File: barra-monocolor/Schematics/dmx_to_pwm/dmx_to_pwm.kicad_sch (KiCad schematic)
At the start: 54 parts, among them J1 RJ45, J2 RJ45, J3 Conn_01x05_Socket, J4 Conn_02x04_Odd_Even, Q1 BD237, Q2 BD237, Q3 BD237, Q4 BD237, SW1 SW_DIP_x08, U1 LM317_TO-220, U2 LM2596T-5, U3 LM337_TO220, U4 LM337_TO220, U5 LM337_TO220, U6 LM337_TO220, U7 SN75176AP, U8 H11L1

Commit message: first pcb layout
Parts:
- removed C10, C11, C8, C9: 1uF, symbol Device:C_Polarized
- removed C2, C3, C4, C5: 100nF, symbol Device:C_Polarized
- removed C6: C_Polarized, symbol Device:C_Polarized
- removed D1, D3, D4, D5, D6: D, symbol Device:D
- removed J3: Conn_01x05_Socket, symbol Connector:Conn_01x05_Socket
- removed J4: Conn_02x04_Odd_Even, symbol Connector_Generic:Conn_02x04_Odd_Even
- removed L1: 100 uH, symbol Device:L
- removed Q1, Q2, Q3, Q4: BD237, Package_TO_SOT_THT:TO-126-3_Vertical, symbol Transistor_BJT:BD237
- removed R11, R12: 470, Resistor_THT:R_Axial_DIN0204_L3.6mm_D1.6mm_P7.62mm_Horizontal, symbol Device:R_US
- removed R5: 8, symbol Device:R_US
- removed R6, R7, R8, R9: 2.7, symbol Device:R
- removed SW1: SW_DIP_x08, symbol Switch:SW_DIP_x08
- removed U1: LM317_TO-220, Package_TO_SOT_THT:TO-220-3_Vertical, symbol Regulator_Linear:LM317_TO-220
- removed U7: SN75176AP, Package_DIP:DIP-8_W7.62mm, symbol Interface_UART:SN75176AP
- removed U8: H11L1, symbol Isolator:H11L1
- added C10, C11, C8, C9: 1uF, Capacitor_THT:C_Disc_D3.0mm_W2.0mm_P2.50mm, symbol Device:C
- added C2, C3, C4, C5: 100nF, Capacitor_THT:C_Disc_D3.0mm_W2.0mm_P2.50mm, symbol Device:C
- added D3, D4, D5, D6: 1N4004, Diode_THT:D_DO-41_SOD81_P7.62mm_Horizontal, symbol Diode:1N4004
- added J3: Conn_02x04_Top_Bottom, Connector_PinHeader_2.54mm:PinHeader_2x04_P2.54mm_Vertical, symbol Connector_Generic:Conn_02x04_Top_Bottom
- added J5: Conn_01x05_Socket, Connector_JST:JST_EH_B5B-EH-A_1x05_P2.50mm_Vertical, symbol Connector:Conn_01x05_Socket
- added L1: 100uH, Capacitor_THT:CP_Radial_D12.5mm_P7.50mm, symbol Device:C_Polarized
- added Q1, Q2, Q3, Q5: TIP41, Package_TO_SOT_THT:TO-220-3_Vertical, symbol Transistor_BJT:TIP41
- added R13: 10K, Resistor_THT:R_Axial_DIN0414_L11.9mm_D4.5mm_P7.62mm_Vertical, symbol Device:R_US
- added R14: 470, Resistor_THT:R_Axial_DIN0414_L11.9mm_D4.5mm_P7.62mm_Vertical, symbol Device:R_US
- added R6, R7, R8, R9: 2.7, Resistor_THT:R_Axial_DIN0411_L9.9mm_D3.6mm_P12.70mm_Horizontal, symbol Device:R_US
- added SW1: SW_DIP_x08, Package_DIP:DIP-16_W7.62mm_LongPads, symbol 74xx:74HCT138
- added U8: SN75176AP, Package_DIP:DIP-8_W7.62mm_Socket_LongPads, symbol Interface_UART:SN75176AP
- added U9: H11L1, Package_DIP:DIP-6_W7.62mm_LongPads, symbol Isolator:H11L1
- C1, C7: value 1 mF -> 47uF - 50V; footprint (none) -> Capacitor_THT:CP_Radial_D7.5mm_P2.50mm
- C13: footprint (none) -> Capacitor_THT:C_Disc_D3.0mm_W2.0mm_P2.50mm
- J2: footprint (none) -> Connector_RJ:RJ45_Amphenol_54602-x08_Horizontal
- R1, R2, R3, R4: footprint (none) -> Resistor_THT:R_Axial_DIN0414_L11.9mm_D4.5mm_P7.62mm_Vertical
- R10: value 10K -> 470; footprint (none) -> Resistor_THT:R_Axial_DIN0414_L11.9mm_D4.5mm_P7.62mm_Vertical
- RV1, RV2, RV3, RV4: footprint (none) -> Potentiometer_THT:Potentiometer_Bourns_3296Z_Horizontal
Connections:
- net 5V: now also U2.4 (FB), C10.1, C11.1, C2.1, C3.1, C4.1, C5.1, C8.1, C9.1, D3.1 (K), D4.1 (K), D5.1 (K), D6.1 (K), J5.3 (Pin_3), L1.2, R14.1, U8.8 (VCC), U9.6
- net DATA+: now also U8.6 (A)
- net DATA-: now also U8.7 (B)
- net GND: now also Q1.3 (E), Q2.3 (E), Q3.3 (E), Q5.3 (E), R13.1, SW1.1 (A0), SW1.2 (A1), SW1.3 (A2), SW1.4 (~{E0}), SW1.5 (~{E1}), SW1.6 (E2), SW1.7 (~{Y7}), SW1.8 (GND), U8.5 (GND), U9.2, U9.5; no longer R10.2
- net LASER1: now also R1.2; no longer R1.1
- net LASER2: now also R2.2; no longer R2.1
- net LASER3: now also R3.2; no longer R3.1
- net LASER4: now also R4.2; no longer R4.1
- net SW1: now also SW1.16 (VCC)
- net SW2: now also SW1.15 (~{Y0})
- net SW3: now also SW1.14 (~{Y1})
- net SW4: now also SW1.13 (~{Y2})
- net SW5: now also SW1.12 (~{Y3})
- net SW6: now also SW1.11 (~{Y4})
- net SW7: now also SW1.10 (~{Y5})
- net SW8: now also SW1.9 (~{Y6})
- net at U6.1 (ADJ): now also RV2.3, C9.2, D4.2 (A), J5.2 (Pin_2); no longer RV4.3
- net at U4.1 (ADJ): now also RV3.3, C10.2, D5.2 (A), J5.4 (Pin_4); no longer RV2.3
- net at U4.3 (VO): now also R8.2
- net at RV2.1, RV2.2: now also R7.1
- net at R10.1: now also U9.1
- net at U3.1 (ADJ): now also RV4.3, C11.2, D6.2 (A), J5.5 (Pin_5); no longer RV1.3
- net at D2.2 (A), U2.2 (OUT): now also L1.1
- net at U4.2 (VI): now also C4.2, J3.7 (Pin_7)
- net at U6.3 (VO): now also R7.2
- net at RV4.1, RV4.2: now also R9.1
- net at U3.3 (VO): now also R9.2
- net at RV1.1, RV1.2: now also R6.1
- net at A1.2 (D0/RX): now also R14.2, U9.4
- net at U5.2 (VI): now also C2.2, J3.5 (Pin_5)
- net at U6.2 (VI): now also C3.2, J3.6 (Pin_6)
- net at U3.2 (VI): now also C5.2, J3.8 (Pin_8)
- net at U5.1 (ADJ): now also RV1.3, C8.2, D3.2 (A), J5.1 (Pin_1); no longer RV3.3
- net at U5.3 (VO): now also R6.2
- net at RV3.1, RV3.2: now also R8.1
- new net: R10.2, U8.1 (R)
- new net: R13.2, U8.2 (~{RE}), U8.3 (DE)
- new net: Q3.1 (B), R4.1
- new net: J3.4 (Pin_4), Q3.2 (C)
- new net: J3.1 (Pin_1), Q5.2 (C)
- new net: J3.2 (Pin_2), Q1.2 (C)
- new net: J3.3 (Pin_3), Q2.2 (C)
- new net: Q5.1 (B), R1.1
- new net: Q2.1 (B), R3.1
- new net: Q1.1 (B), R2.1
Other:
- note added: "ORANGE IN RJ45"
- note added: "WHITE/ORANGE IN RJ45"
- note removed: "BLUE IN PROTOTYPE (WHITE/ORANGE IN RJ45)"
- note removed: "GREEN IN PROTOTYPE (ORANGE IN RJ45)"

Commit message: added board
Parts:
- R14: value 470 -> 1K
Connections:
- net VIN is gone; now on net VCC: C1.1, U2.1 (VIN)
- net GND: now also D2.2 (A); no longer D2.1 (K)
- net L2-SOC-OUT: now reaches C3.2, J3.6 (Pin_6), U6.2 (VI)
- net L3-SOC-OUT: now reaches J3.4 (Pin_4)
- net L3-SOC-OUT: now also C4.2, U4.2 (VI); no longer Q3.2 (C)
- net L4-SOC-OUT: now reaches C5.2, U3.2 (VI)
- net L4-SOC-OUT: now also J3.2 (Pin_2); no longer J3.8 (Pin_8)
- net L1-SOC-IN: now reaches Q5.2 (C)
- net L1-SOC-IN: now also J3.7 (Pin_7); no longer J3.1 (Pin_1)
- net L2-SOC-IN: now reaches Q1.2 (C)
- net L2-SOC-IN: now also J3.5 (Pin_5); no longer J3.2 (Pin_2)
- net L3-SOC-IN: now reaches J3.3 (Pin_3), Q2.2 (C)
- net L1-SOC-OUT: now reaches C2.2, U5.2 (VI)
- net L1-SOC-OUT: now also J3.8 (Pin_8); no longer J3.5 (Pin_5)
- net at L1.1, U2.2 (OUT): now also D2.1 (K); no longer D2.2 (A)
- new net L4-SOC-IN: J3.1 (Pin_1), Q3.2 (C)
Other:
- moved on the sheet: C10, C11, C4, C5, D2, D5, D6, J3, Q1, Q2, Q3, Q5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

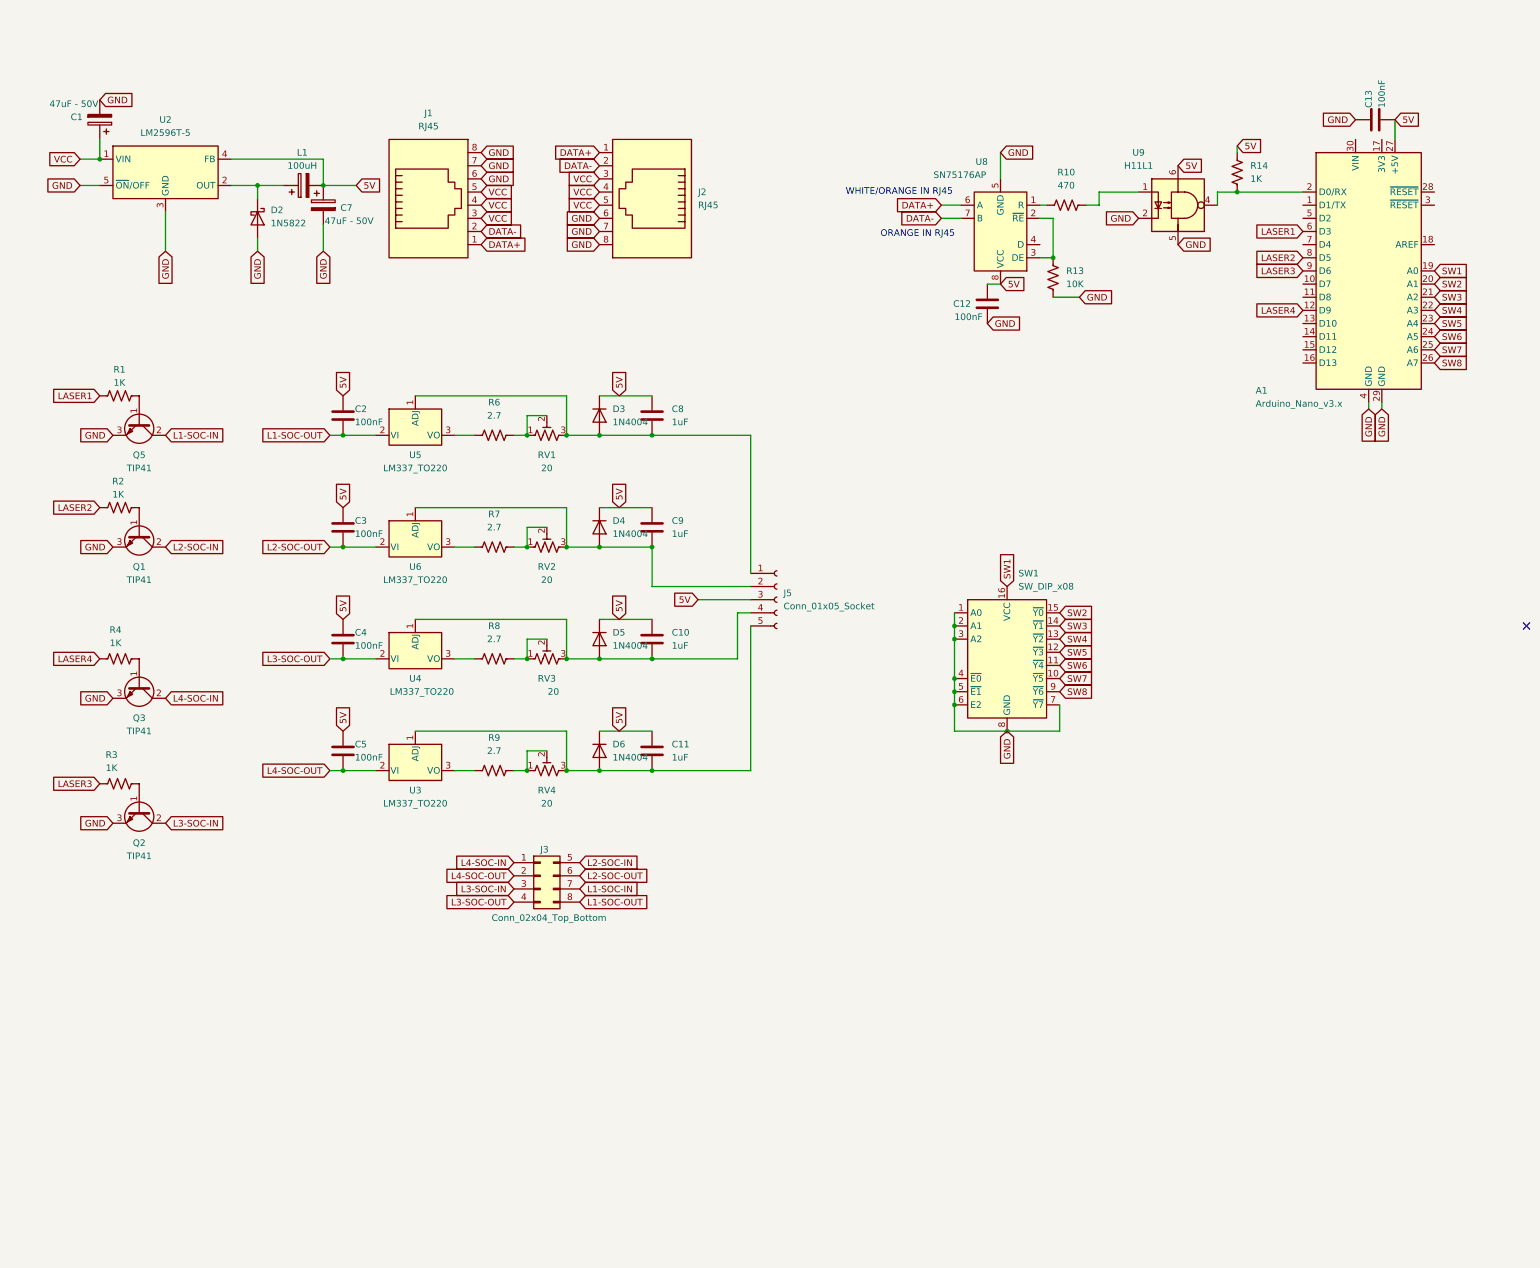
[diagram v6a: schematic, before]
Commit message: improved pcb track width, added antenna connector
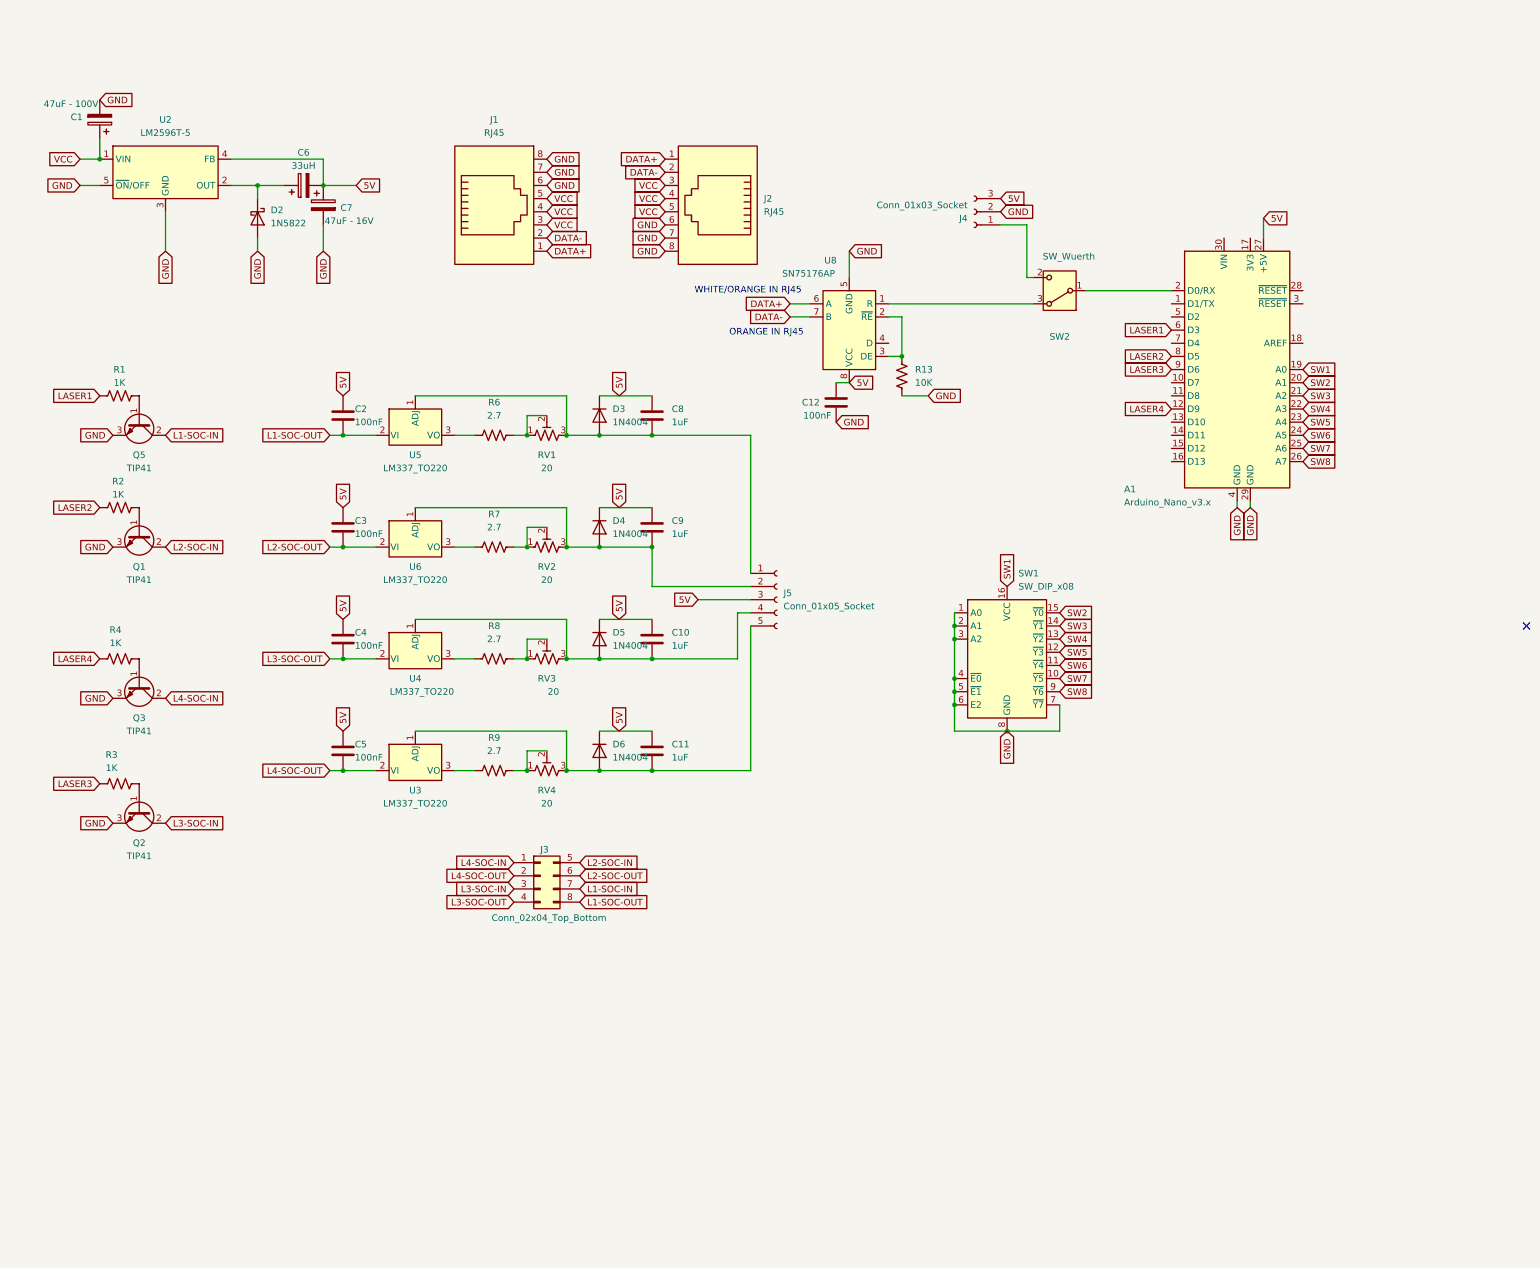
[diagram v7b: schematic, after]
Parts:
- removed C13: 100nF, Capacitor_THT:C_Disc_D3.0mm_W2.0mm_P2.50mm, symbol Device:C
- removed L1: 100uH, Capacitor_THT:CP_Radial_D12.5mm_P7.50mm, symbol Device:C_Polarized
- removed R10: 470, Resistor_THT:R_Axial_DIN0414_L11.9mm_D4.5mm_P7.62mm_Vertical, symbol Device:R_US
- removed R14: 1K, Resistor_THT:R_Axial_DIN0414_L11.9mm_D4.5mm_P7.62mm_Vertical, symbol Device:R_US
- removed U9: H11L1, Package_DIP:DIP-6_W7.62mm_LongPads, symbol Isolator:H11L1
- added C6: 33uH, Capacitor_THT:CP_Radial_D8.0mm_P5.00mm, symbol Device:C_Polarized
- added J4: Conn_01x03_Socket, Connector_JST:JST_EH_B3B-EH-A_1x03_P2.50mm_Vertical, symbol Connector:Conn_01x03_Socket
- added SW2: SW_Wuerth, Button_Switch_THT:SW_Slide-03_Wuerth-WS-SLTV_10x2.5x6.4_P2.54mm, symbol Switch:SW_Wuerth_450301014042
- C1: value 47uF - 50V -> 47uF - 100V
- C7: value 47uF - 50V -> 47uF - 16V
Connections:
- net 5V: now also C6.2, J4.3 (Pin_3)
- net GND: now also J4.2 (Pin_2)
- net at U8.1 (R): now also SW2.3 (A)
- net at A1.2 (D0/RX): now also SW2.1 (B)
- net at D2.1 (K), U2.2 (OUT): now also C6.1
- new net: J4.1 (Pin_1), SW2.2 (C)
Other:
- moved on the sheet: A1, C12, J1, J2, R13, U8

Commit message: stuff
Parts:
- removed D5: 1N4004, Diode_THT:D_DO-41_SOD81_P7.62mm_Horizontal, symbol Diode:1N4004
- removed U3, U4, U5, U6: LM337_TO220, Package_TO_SOT_THT:TO-220-3_Vertical, symbol Regulator_Linear:LM337_TO220
- added D1: 1N4004, Diode_THT:D_DO-41_SOD81_P7.62mm_Horizontal, symbol Diode:1N4004
- added H1, H2, H3, H4, H5: MountingHole_Pad, MountingHole:MountingHole_3.2mm_M3_Pad, symbol Mechanical:MountingHole_Pad
- added U1, U3, U4, U5: LM317_TO-220, Package_TO_SOT_THT:TO-220-3_Vertical, symbol Regulator_Linear:LM317_TO-220
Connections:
- net 5V: now also Q1.2 (C), Q2.2 (C), Q3.2 (C), Q5.2 (C); no longer C10.1, C11.1, C2.1, C3.1, C4.1, C5.1, C8.1, C9.1, D3.1 (K), D4.1 (K), D6.1 (K), J5.3 (Pin_3)
- net GND: now also C10.1, C11.1, C2.1, C3.1, C4.1, C5.1, C8.1, C9.1, D3.2 (A), D4.2 (A), D6.2 (A), J5.3 (Pin_3), D1.2 (A), H5.1; no longer Q1.3 (E), Q2.3 (E), Q3.3 (E), Q5.3 (E)
- net L1-SOC-IN: now also Q5.3 (E); no longer Q5.2 (C)
- net L1-SOC-OUT: now also U5.3 (VI)
- net L2-SOC-IN: now also Q1.3 (E); no longer Q1.2 (C)
- net L2-SOC-OUT: now also U4.3 (VI)
- net L3-SOC-IN: now also Q2.3 (E); no longer Q2.2 (C)
- net L3-SOC-OUT: now also U3.3 (VI)
- net L4-SOC-IN: now also Q3.3 (E); no longer Q3.2 (C)
- net L4-SOC-OUT: now also U1.3 (VI)
- net at R7.2: now also U4.2 (VO)
- net at C9.2, J5.2 (Pin_2), RV2.3: now also D3.1 (K), U4.1 (ADJ); no longer D4.2 (A)
- net at R6.2: now also U5.2 (VO)
- net at C11.2, J5.5 (Pin_5), RV4.3: now also D6.1 (K), U1.1 (ADJ); no longer D6.2 (A)
- net at C10.2, J5.4 (Pin_4), RV3.3: now also D1.1 (K), U3.1 (ADJ)
- net at R8.2: now also U3.2 (VO)
- net at C8.2, J5.1 (Pin_1), RV1.3: now also D4.1 (K), U5.1 (ADJ); no longer D3.2 (A)
- net at R9.2: now also U1.2 (VO)
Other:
- moved on the sheet: D6, Q1, Q2, Q3, Q5, R1, R2, R3, R4
